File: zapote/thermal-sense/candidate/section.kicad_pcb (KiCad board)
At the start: 2 copper layers, 100 x 45 mm, 27 parts, among them J1 B2B-XH-A(LF)(SN), J2 B2B-XH-A(LF)(SN), J3 B6B-XH-A(LF)(SN), U1 TLV3201AIDBVR, U2 TLV3201AIDBVR, U3 TLV9031DBVR, U4 TLV9031DBVR, U5 SN74LVC1G32DBVR, U6 SN74LVC1G32DBVR

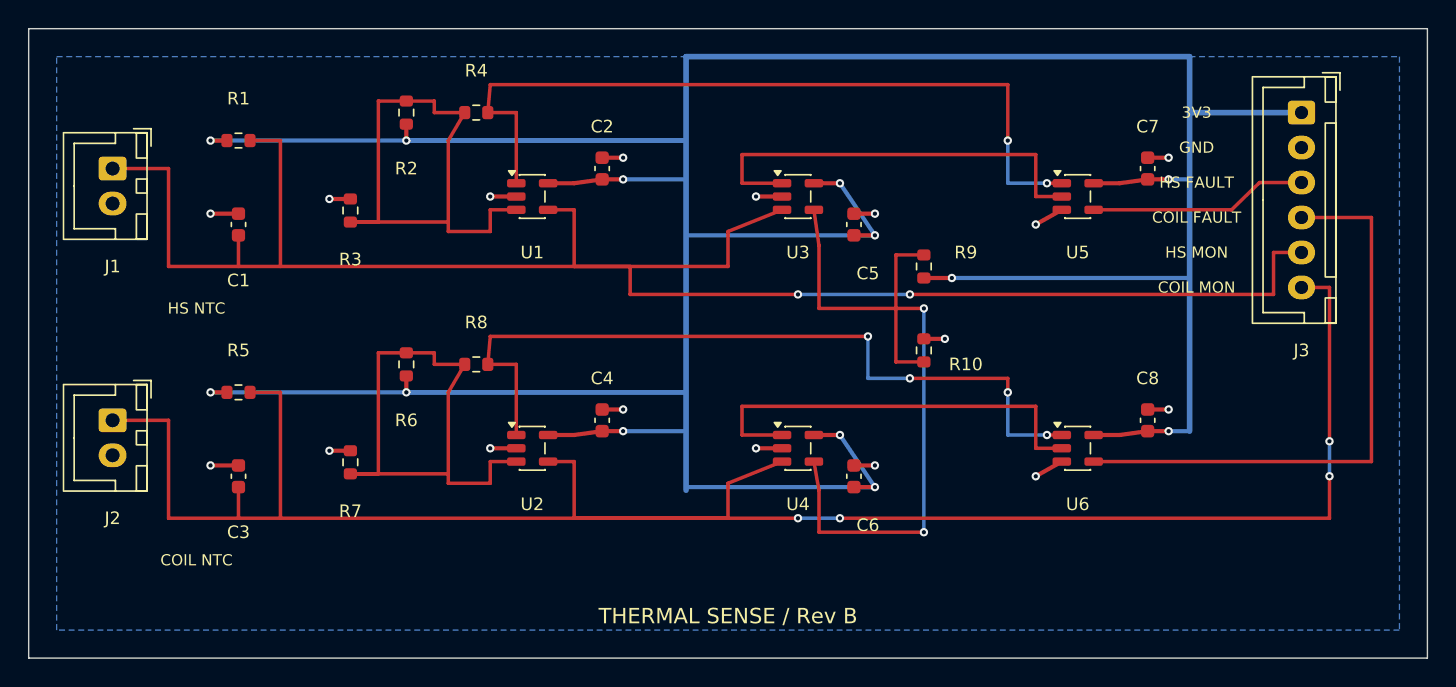
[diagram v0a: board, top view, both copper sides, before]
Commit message: fix(zapote): JLC pad/inner-layer limits; unit silk legends meet JLC minimums (#1679)
* feat(zapote-drc): JLC pad-to-pad, pad-to-track and inner-layer PTH limits

Re-read verbatim from the capabilities page:
- "SMD pad to pad clearance (different nets) 0.15mm" (all profiles)
- "Pad to track clearance (1oz) 0.1mm" (4L 1 oz)
- "Inner layer PTH pad hole to copper clearance 0.3mm" (4-layer)

Pad-specific clearance rules follow the general spacing so KiCad's
last-match-wins judges a pad pair by its own row; the interlock U4 pads
(0.15 mm) now pass. Inner-layer rule uses (layer inner); arcs are 'Track'
in KiCad expressions (measured). The self-test board is now 4-layer and
exercises all 11 rules; fixture report regenerated from the real rules.

Co-Authored-By: Claude Opus 5.5 (1M context) <noreply@anthropic.com>

* fix(zapote): unit silk legends meet JLC minimums (4 of 5 units)

current-sense, thermal-sense, interlock and gate-drive silkscreen text is
raised to 1.0 mm / 0.15 mm (tools/silk_legend_minimums.py; character width
kept so narrow label columns stay clear; current-sense R4 refdes moved
above the part). All four pass the fab pass; native ERC/DRC stay clean.

Native exports are re-recorded under evidence/silk-legend-2026-10-08/ and
units.json points at them: the extractor's output is identical for the old
and new boards apart from board identity, the current-sense composite
builder reproduces the old composite byte for byte, and live check-units
findings are unchanged per unit. Historical evidence is left in place.

RTD is deferred: its model-qualification receipt binds the board bytes and
needs the model-correctness replay, not a hand re-bind.

Co-Authored-By: Claude Opus 5.5 (1M context) <noreply@anthropic.com>

---------

Co-authored-by: Claude Opus 5.5 (1M context) <noreply@anthropic.com>
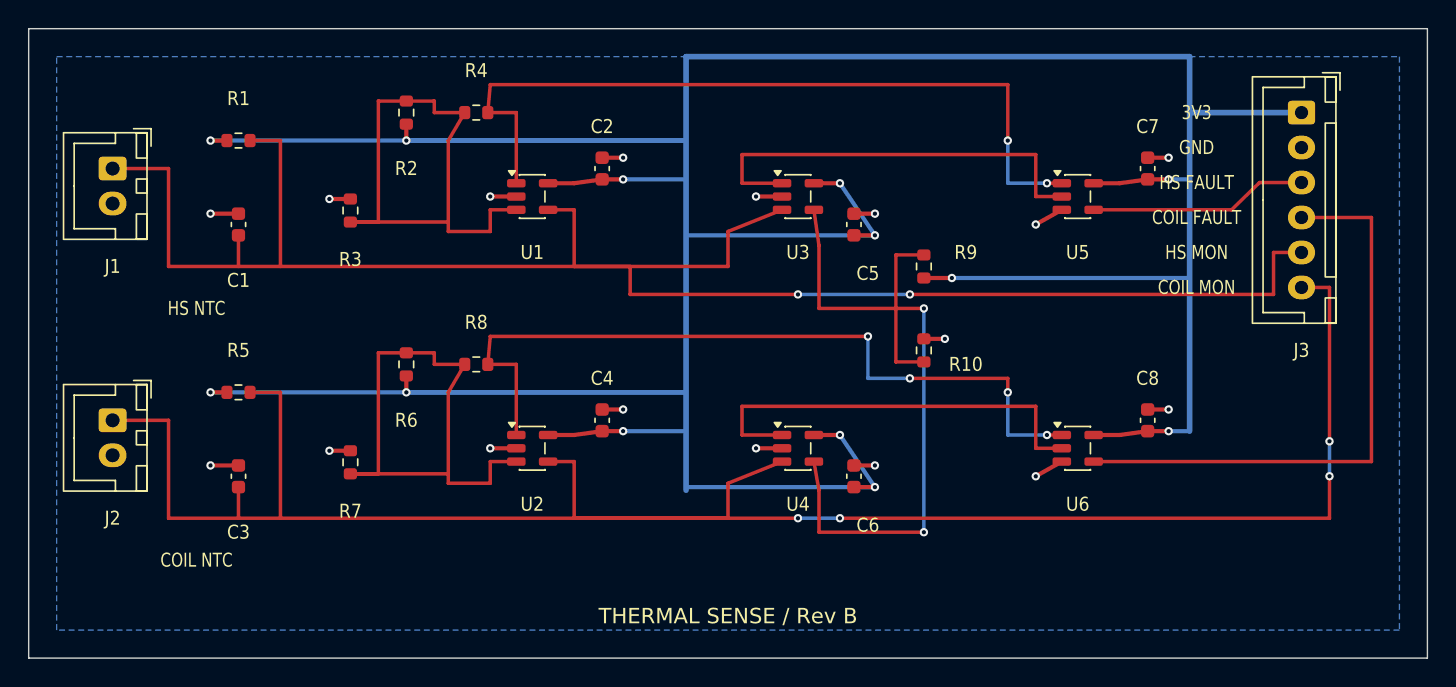
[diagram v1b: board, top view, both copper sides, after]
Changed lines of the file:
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@@
 			(effects
 				(font
-					(size 0.9 0.9)
-					(thickness 0.12)
+					(size 1 0.9)
+					(thickness 0.15)
 				)
 			)
@@
 			(effects
 				(font
-					(size 0.9 0.9)
-					(thickness 0.12)
+					(size 1 0.9)
+					(thickness 0.15)
 				)
 			)
@@
 			(effects
 				(font
-					(size 0.9 0.9)
-					(thickness 0.12)
+					(size 1 0.9)
+					(thickness 0.15)
 				)
 			)
@@
 			(effects
 				(font
-					(size 0.9 0.9)
-					(thickness 0.12)
+					(size 1 0.9)
+					(thickness 0.15)
 				)
 			)
@@
 			(effects
 				(font
-					(size 0.9 0.9)
-					(thickness 0.12)
+					(size 1 0.9)
+					(thickness 0.15)
 				)
 			)
@@
 			(effects
 				(font
-					(size 0.9 0.9)
-					(thickness 0.12)
+					(size 1 0.9)
+					(thickness 0.15)
 				)
 			)
@@
 			(effects
 				(font
-					(size 0.9 0.9)
-					(thickness 0.12)
+					(size 1 0.9)
+					(thickness 0.15)
 				)
 			)
@@
 			(effects
 				(font
-					(size 0.9 0.9)
-					(thickness 0.12)
+					(size 1 0.9)
+					(thickness 0.15)
 				)
 			)
@@
 			(effects
 				(font
-					(size 0.9 0.9)
-					(thickness 0.12)
+					(size 1 0.9)
+					(thickness 0.15)
 				)
 			)
@@
 			(effects
 				(font
-					(size 0.9 0.9)
-					(thickness 0.12)
+					(size 1 0.9)
+					(thickness 0.15)
 				)
 			)
@@
 			(effects
 				(font
-					(size 0.9 0.9)
-					(thickness 0.12)
+					(size 1 0.9)
+					(thickness 0.15)
 				)
 			)
@@
 			(effects
 				(font
-					(size 0.9 0.9)
-					(thickness 0.12)
+					(size 1 0.9)
+					(thickness 0.15)
 				)
 			)
@@
 			(effects
 				(font
-					(size 0.9 0.9)
-					(thickness 0.12)
+					(size 1 0.9)
+					(thickness 0.15)
 				)
 			)
@@
 			(effects
 				(font
-					(size 0.9 0.9)
-					(thickness 0.12)
+					(size 1 0.9)
+					(thickness 0.15)
 				)
 			)
@@
 			(effects
 				(font
-					(size 0.9 0.9)
-					(thickness 0.12)
+					(size 1 0.9)
+					(thickness 0.15)
 				)
 			)
@@
 			(effects
 				(font
-					(size 0.9 0.9)
-					(thickness 0.12)
+					(size 1 0.9)
+					(thickness 0.15)
 				)
 			)
@@
 			(effects
 				(font
-					(size 0.9 0.9)
-					(thickness 0.12)
+					(size 1 0.9)
+					(thickness 0.15)
 				)
 			)
@@
 			(effects
 				(font
-					(size 0.9 0.9)
-					(thickness 0.12)
+					(size 1 0.9)
+					(thickness 0.15)
 				)
 			)
@@
 			(effects
 				(font
-					(size 0.9 0.9)
-					(thickness 0.12)
+					(size 1 0.9)
+					(thickness 0.15)
 				)
 			)
@@
 			(effects
 				(font
-					(size 0.9 0.9)
-					(thickness 0.12)
+					(size 1 0.9)
+					(thickness 0.15)
 				)
 			)
@@
 			(effects
 				(font
-					(size 0.9 0.9)
-					(thickness 0.12)
+					(size 1 0.9)
+					(thickness 0.15)
 				)
 			)
@@
 			(effects
 				(font
-					(size 0.9 0.9)
-					(thickness 0.12)
+					(size 1 0.9)
+					(thickness 0.15)
 				)
 			)
@@
 			(effects
 				(font
-					(size 0.9 0.9)
-					(thickness 0.12)
+					(size 1 0.9)
+					(thickness 0.15)
 				)
 			)
@@
 			(effects
 				(font
-					(size 0.9 0.9)
-					(thickness 0.12)
+					(size 1 0.9)
+					(thickness 0.15)
 				)
 			)
@@
 			(effects
 				(font
-					(size 0.9 0.9)
-					(thickness 0.12)
+					(size 1 0.9)
+					(thickness 0.15)
 				)
 			)
@@
 			(effects
 				(font
-					(size 0.9 0.9)
-					(thickness 0.12)
+					(size 1 0.9)
+					(thickness 0.15)
 				)
 			)
@@
 			(effects
 				(font
-					(size 0.9 0.9)
-					(thickness 0.12)
+					(size 1 0.9)
+					(thickness 0.15)
 				)
 			)
@@
 		(effects
 			(font
-				(size 0.8 0.8)
-				(thickness 0.12)
+				(size 1 0.8)
+				(thickness 0.15)
 			)
 		)
@@
 		(effects
 			(font
-				(size 0.8 0.8)
-				(thickness 0.12)
+				(size 1 0.8)
+				(thickness 0.15)
 			)
 		)
@@
 		(effects
 			(font
-				(size 0.8 0.8)
-				(thickness 0.12)
+				(size 1 0.8)
+				(thickness 0.15)
 			)
 		)
@@
 		(effects
 			(font
-				(size 0.8 0.8)
-				(thickness 0.12)
+				(size 1 0.8)
+				(thickness 0.15)
 			)
 		)
@@
 		(effects
 			(font
-				(size 0.8 0.8)
-				(thickness 0.12)
+				(size 1 0.8)
+				(thickness 0.15)
 			)
 		)
@@
 		(effects
 			(font
-				(size 0.8 0.8)
-				(thickness 0.12)
+				(size 1 0.8)
+				(thickness 0.15)
 			)
 		)
@@
 		(effects
 			(font
-				(size 0.8 0.8)
-				(thickness 0.12)
+				(size 1 0.8)
+				(thickness 0.15)
 			)
 		)
@@
 		(effects
 			(font
-				(size 0.8 0.8)
-				(thickness 0.12)
+				(size 1 0.8)
+				(thickness 0.15)
 			)
 		)
@@
 			(font
 				(size 1.1 1.1)
-				(thickness 0.12)
+				(thickness 0.15)
 			)
 		)
